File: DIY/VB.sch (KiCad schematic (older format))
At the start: 6 parts, among them J1 Barrel_Jack, J2 Virtual Boy ctrl slot, J3 DB25_Male, SW1 SW_SPST, U1 74AHCT125N, U2 74AHCT125N

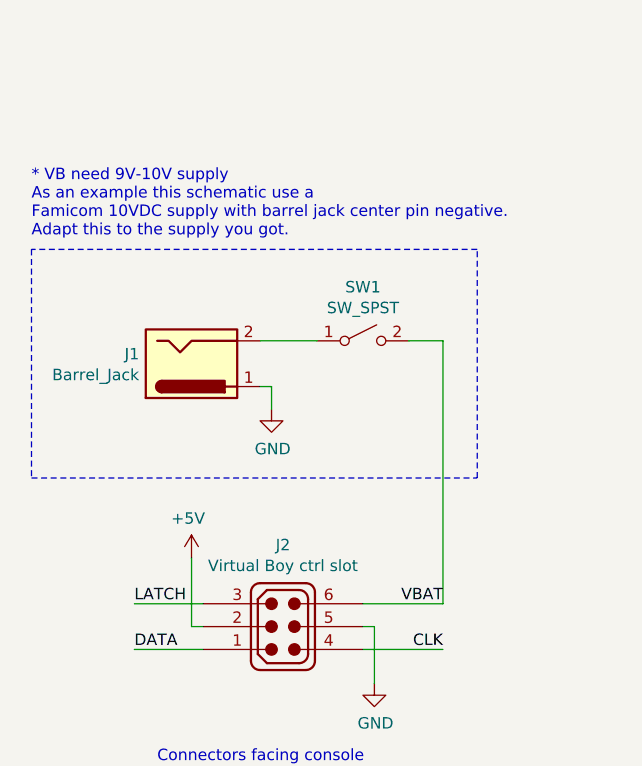
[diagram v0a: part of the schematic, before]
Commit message: Simplify parallel schematics
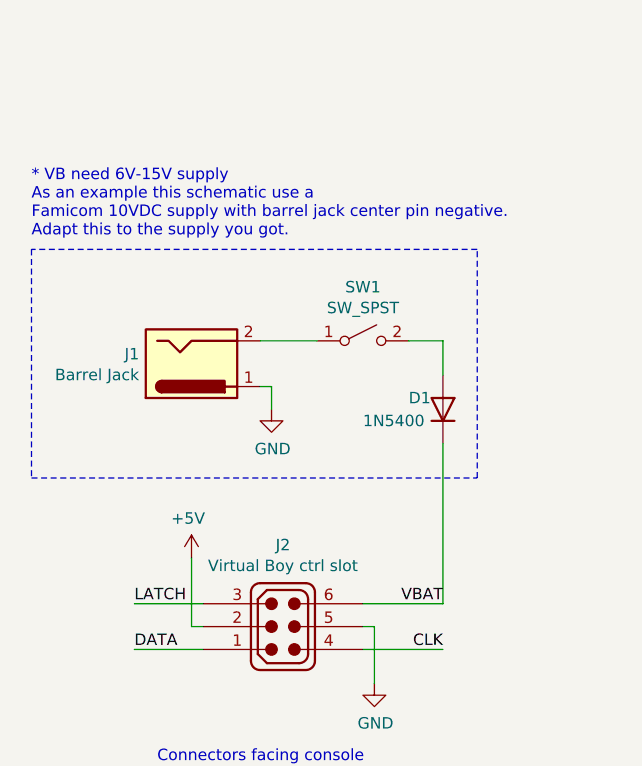
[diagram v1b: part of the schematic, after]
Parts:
- added D1: 1N5400, Diode_THT:D_DO-201AD_P15.24mm_Horizontal, symbol Diode:1N5400
- J1: value Barrel_Jack -> Barrel Jack
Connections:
- net VBAT: now also D1.1 (K); no longer SW1.2 (B)
- new net: D1.2 (A), SW1.2 (B)
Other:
- note added: "* VB need 6V-15V supply\nAs an example this schematic use a\nFamicom 10VDC supply with barrel jack center pin negative.\nAdapt this to the supply you got."
- note removed: "* VB need 9V-10V supply\nAs an example this schematic use a\nFamicom 10VDC supply with barrel jack center pin negative.\nAdapt this to the supply you got."
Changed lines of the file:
@@
 $Descr USLetter 11000 8500
 encoding utf-8
-Sheet 17 19
+Sheet 17 20
 Title "BlueRetro - Virtual Boy adapter cable"
 Date "2022-01-10"
 Rev "v1.0"
-Comp "©2022 Jacques Gagnon, licensed under CC-BY-4.0"
+Comp "©2020-2022 Jacques Gagnon, licensed under CC-BY-4.0"
 Comment1 ""
 Comment2 ""
@@
 P 2000 2700
 F 0 "J1" H 1771 2658 50  0000 R CNN
-F 1 "Barrel_Jack" H 1771 2749 50  0000 R CNN
+F 1 "Barrel Jack" H 1771 2749 50  0000 R CNN
 F 2 "" H 2050 2660 50  0001 C CNN
 F 3 "~" H 2050 2660 50  0001 C CNN
@@
 Wire Wire Line
 	2950 2600 3100 2600
-Wire Wire Line
-	3100 2600 3100 3750
 Wire Wire Line
 	3100 3750 2750 3750
@@
 	1300 2200 1300 3200
 Text Notes 1300 2150 0    50   ~ 0
-* VB need 9V-10V supply\nAs an example this schematic use a\nFamicom 10VDC supply with barrel jack center pin negative.\nAdapt this to the supply you got.
+* VB need 6V-15V supply\nAs an example this schematic use a\nFamicom 10VDC supply with barrel jack center pin negative.\nAdapt this to the supply you got.
+$Comp
+L Diode:1N5400 D1
+U 1 1 62235F33
+P 3100 2900
+F 0 "D1" V 3150 2750 50  0000 L CNN
+F 1 "1N5400" V 3050 2550 50  0000 L CNN
+F 2 "Diode_THT:D_DO-201AD_P15.24mm_Horizontal" H 3100 2725 50  0001 C CNN
+F 3 "http://www.vishay.com/docs/88516/1n5400.pdf" H 3100 2900 50  0001 C CNN
+	1    3100 2900
+	0    1    -1   0
+$EndComp
+Wire Wire Line
+	3100 2600 3100 2750
+Wire Wire Line
+	3100 3050 3100 3750
 $EndSCHEMATC

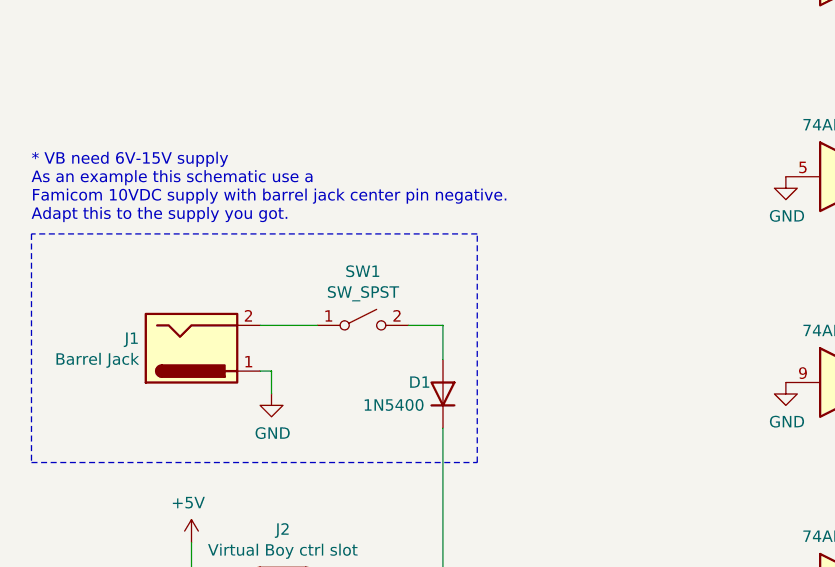
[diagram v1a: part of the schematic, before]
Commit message: Change VB schem to use barrel center pin positive
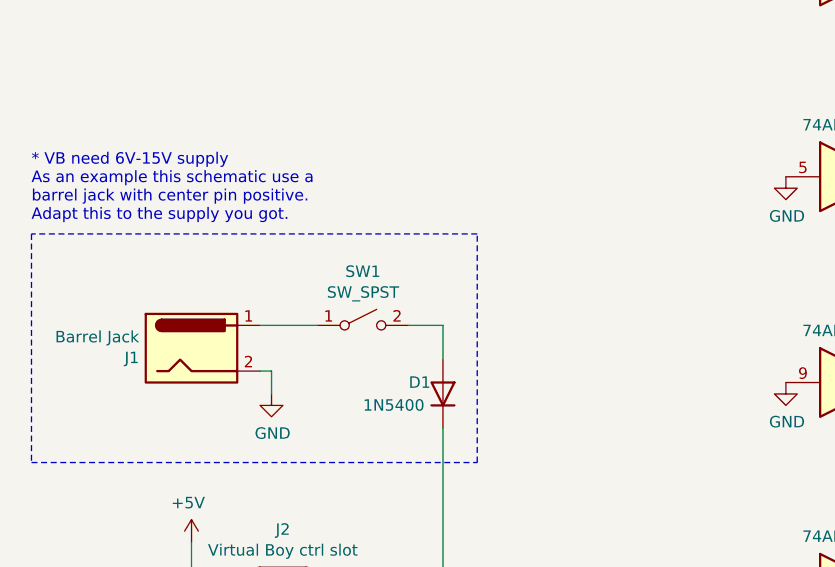
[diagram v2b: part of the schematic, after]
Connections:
- net GND: now also J1.2; no longer J1.1
- net at SW1.1 (A): now also J1.1; no longer J1.2
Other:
- note added: "* VB need 6V-15V supply\nAs an example this schematic use a\nbarrel jack with center pin positive.\nAdapt this to the supply you got."
- note removed: "* VB need 6V-15V supply\nAs an example this schematic use a\nFamicom 10VDC supply with barrel jack center pin negative.\nAdapt this to the supply you got."
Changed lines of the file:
@@
 F 3 "~" H 2050 2660 50  0001 C CNN
 	1    2000 2700
-	1    0    0    1
+	1    0    0    -1
 $EndComp
 $Comp
@@
 	1300 2200 1300 3200
 Text Notes 1300 2150 0    50   ~ 0
-* VB need 6V-15V supply\nAs an example this schematic use a\nFamicom 10VDC supply with barrel jack center pin negative.\nAdapt this to the supply you got.
+* VB need 6V-15V supply\nAs an example this schematic use a\nbarrel jack with center pin positive.\nAdapt this to the supply you got.
 $Comp
 L Diode:1N5400 D1
